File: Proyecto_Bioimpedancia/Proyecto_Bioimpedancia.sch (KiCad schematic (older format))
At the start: 53 parts

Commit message: Esquematico con Huellas
Anexado huella pulsador
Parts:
- SW?: footprint (none) -> Huellas:KPT_1187B
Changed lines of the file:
@@
 F 0 "SW?" H 8150 2810 50  0000 C CNN
 F 1 "SW_PUSH" H 8000 2620 50  0000 C CNN
-F 2 "" H 8000 2700 50  0000 C CNN
+F 2 "Huellas:KPT_1187B" H 8000 2700 50  0001 C CNN
 F 3 "" H 8000 2700 50  0000 C CNN
 	1    8000 2700

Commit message: Esquematico Actualizado
Cambios Sugeridos y división en sub-bloques
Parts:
- removed R? (x2): 10K, Resistors_SMD:R_0805_HandSoldering, symbol 10K
- added J? (x2): Jumper, Pin_Headers:Pin_Header_Straight_1x02_Pitch2.54mm, symbol Jumper
- added R? (x2): 10K, Resistors_SMD:R_0805_HandSoldering, symbol 10K
- D1: renamed from D?; footprint (none) -> LEDs:LED_0805
- R5: renamed from R?; value R_Small -> R_CAL
- U5: renamed from U?; footprint TO_SOT_Packages_SMD:SOT-223-3Lead_TabPin2 -> TO_SOT_Packages_SMD:SOT-223
- gave numbers to parts that had none: 47
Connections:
- net labels added: FEEDBACK_A2, RFB_AD5933, SIGNAL_A1, SIGNAL_A2, VIN_AD5933, VOUT_AD5933
- net labels removed: OUT_OPAMB, RFB
- wire segments 151 -> 158
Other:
- note added: "Amplicador A2"
- note added: "Amplificador A1"
- note added: "Bioimpedanciometro"
- note added: "Conector Bootloader"
- note added: "Conector Progrmador \ndel Microcontrolador"
- note added: "Microcontrolador"
- note added: "Oscilador AD5933"
- note added: "Pines de Alimentación y Control"
- note added: "Pulsador Reset"
- note added: "Regulador"
- note added: "Resistencias Pull-up"
- note added: "Señal de Reloj Externo"
- note added: "Switch Medida Bioimpedancia"
- moved on the sheet: C1, C10, C11, C12, C13, C2, C20, C3, C4, D1, P1, R1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

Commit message: Diseño Mejorado 10/05/2017
Diagrama mas explicativo con señales mas claras
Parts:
- added J1: Jumper_Calibration, Pin_Headers:Pin_Header_Straight_1x02_Pitch2.54mm, symbol Jumper
- R5: value R_CAL -> R_GAIN; footprint (none) -> Resistors_SMD:R_0805_HandSoldering
- R8: footprint (none) -> Resistors_SMD:R_0805_HandSoldering
- W1, W2, W3, W4, W5, W6: footprint (none) -> Measurement_Points:Measurement_Point_Round-TH_Small
- Y1: footprint Huellas:AMB3_Crystal_5mm_x_3,2mm_16M -> Crystals:Crystal_SMD_Abracon_ABM3-2pin_5.0x3.2mm_HandSoldering
- gave numbers to parts that had none: 4
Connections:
- net labels added: CTRL_MCLK, CTRL_SWITCH
- net labels removed: ADC2, ADC3, IN_OPAMB, OUT_OPAM1, VIN, VOUT
- wire segments 158 -> 160
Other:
- note added: "Amplificador A2"
- note added: "Electrodos de Contacto y R de Calibración"
- note added: "Oscilador AD5933 (MCLK)"
- note added: "Quemador Bootloader"
- note added: "Señales Analogicas (Medición)"
- note removed: "Amplicador A2"
- note removed: "Conector Bootloader"
- note removed: "Oscilador AD5933"
- note removed: "Señales Analogicos"
- moved on the sheet: P3, P4
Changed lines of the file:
@@
 	1    0    0    -1
 $EndComp
-Text Notes 2450 650  0    118  ~ 0
-Señales Analogicos
 $Comp
 L 0,1uF C15
@@
 MCLK
 Text Label 8150 1450 0    39   ~ 0
-ADC3
+CTRL_MCLK
 Text Label 8800 2700 0    39   ~ 0
-ADC3
+CTRL_MCLK
 Text Label 8800 2900 0    39   ~ 0
 GND
@@
 SIGNAL_A1
 Text Label 4000 1350 0    39   ~ 0
-ADC2
+CTRL_SWITCH
 Text Label 4250 1550 0    39   ~ 0
 AGND
@@
 ADC1
 Text Label 8150 1350 0    39   ~ 0
-ADC2
+CTRL_SWITCH
 Text Label 8150 1750 0    39   ~ 0
 RESET
@@
 F 0 "R8" H 5530 1370 50  0000 L CNN
 F 1 "RCAL" H 5250 1350 50  0000 L CNN
-F 2 "" H 5500 1350 50  0000 C CNN
+F 2 "Resistors_SMD:R_0805_HandSoldering" H 5500 1350 50  0001 C CNN
 F 3 "" H 5500 1350 50  0000 C CNN
 	1    5500 1350
@@
 P 1550 2450
 F 0 "R5" H 1580 2470 50  0000 L CNN
-F 1 "R_CAL" H 1580 2410 50  0000 L CNN
-F 2 "" H 1550 2450 50  0000 C CNN
+F 1 "R_GAIN" H 1580 2410 50  0000 L CNN
+F 2 "Resistors_SMD:R_0805_HandSoldering" H 1550 2450 50  0001 C CNN
 F 3 "" H 1550 2450 50  0000 C CNN
 	1    1550 2450
@@
 F 0 "Y1" H 6700 2800 50  0000 C CNN
 F 1 "AMB3_16M" H 6700 2600 50  0000 C CNN
-F 2 "Huellas:AMB3_Crystal_5mm_x_3,2mm_16M" H 6700 2700 50  0001 C CNN
+F 2 "Crystals:Crystal_SMD_Abracon_ABM3-2pin_5.0x3.2mm_HandSoldering" H 6700 2700 50  0001 C CNN
 F 3 "" H 6700 2700 50  0000 C CNN
 	1    6700 2700
@@
 L CONN_01X02 P3
 U 1 1 59144527
-P 7000 4650
-F 0 "P3" H 7000 4800 50  0000 C CNN
-F 1 "CONN_01X02" V 7100 4650 50  0000 C CNN
-F 2 "Socket_Strips:Socket_Strip_Straight_1x02_Pitch2.54mm" H 7000 4650 50  0001 C CNN
-F 3 "" H 7000 4650 50  0000 C CNN
-	1    7000 4650
+P 7000 4500
+F 0 "P3" H 7000 4650 50  0000 C CNN
+F 1 "CONN_01X02" V 7100 4500 50  0000 C CNN
+F 2 "Socket_Strips:Socket_Strip_Straight_1x02_Pitch2.54mm" H 7000 4500 50  0001 C CNN
+F 3 "" H 7000 4500 50  0000 C CNN
+	1    7000 4500
 	1    0    0    -1
 $EndComp
@@
 L CONN_01X02 P4
 U 1 1 59144600
-P 7900 4650
-F 0 "P4" H 7900 4800 50  0000 C CNN
-F 1 "CONN_01X02" V 8000 4650 50  0000 C CNN
-F 2 "Socket_Strips:Socket_Strip_Straight_1x02_Pitch2.54mm" H 7900 4650 50  0001 C CNN
-F 3 "" H 7900 4650 50  0000 C CNN
-	1    7900 4650
-	1    0    0    -1
-$EndComp
-Text Label 7350 4600 0    39   ~ 0
+P 8400 5350
+F 0 "P4" H 8400 5500 50  0000 C CNN
+F 1 "CONN_01X02" V 8500 5350 50  0000 C CNN
+F 2 "Socket_Strips:Socket_Strip_Straight_1x02_Pitch2.54mm" H 8400 5350 50  0001 C CNN
+F 3 "" H 8400 5350 50  0000 C CNN
+	1    8400 5350
+	1    0    0    -1
+$EndComp
+Text Label 7850 5300 0    39   ~ 0
 Z_UK
-Text Label 7350 4700 0    39   ~ 0
-IN_OPAMB
-Text Label 6350 4600 0    39   ~ 0
+Text Label 7850 5400 0    39   ~ 0
+SIGNAL_A2
+Text Label 6350 4450 0    39   ~ 0
 V_FUENTE
-Text Label 6350 4700 0    39   ~ 0
+Text Label 6350 4550 0    39   ~ 0
 AGND
 $Comp
@@
 F 0 "W1" H 1300 4670 50  0000 C CNN
 F 1 "TEST_1P" H 1300 4600 50  0000 C CNN
-F 2 "" H 1500 4400 50  0000 C CNN
+F 2 "Measurement_Points:Measurement_Point_Round-TH_Small" H 1500 4400 50  0001 C CNN
 F 3 "" H 1500 4400 50  0000 C CNN
 	1    1300 4400
@@
 F 0 "W2" H 1650 4670 50  0000 C CNN
 F 1 "TEST_1P" H 1650 4600 50  0000 C CNN
-F 2 "" H 1850 4400 50  0000 C CNN
+F 2 "Measurement_Points:Measurement_Point_Round-TH_Small" H 1850 4400 50  0001 C CNN
 F 3 "" H 1850 4400 50  0000 C CNN
 	1    1650 4400
@@
 F 0 "W3" H 2000 4670 50  0000 C CNN
 F 1 "TEST_1P" H 2000 4600 50  0000 C CNN
-F 2 "" H 2200 4400 50  0000 C CNN
+F 2 "Measurement_Points:Measurement_Point_Round-TH_Small" H 2200 4400 50  0001 C CNN
 F 3 "" H 2200 4400 50  0000 C CNN
 	1    2000 4400
@@
 F 0 "W4" H 2350 4670 50  0000 C CNN
 F 1 "TEST_1P" H 2350 4600 50  0000 C CNN
-F 2 "" H 2550 4400 50  0000 C CNN
+F 2 "Measurement_Points:Measurement_Point_Round-TH_Small" H 2550 4400 50  0001 C CNN
 F 3 "" H 2550 4400 50  0000 C CNN
 	1    2350 4400
@@
 $EndComp
 Text Label 1300 5100 1    39   ~ 0
-OUT_OPAM1
+SIGNAL_A1
 Text Label 1650 5100 1    39   ~ 0
-VOUT
+VOUT_AD5933
 Text Label 2000 5100 1    39   ~ 0
-IN_OPAMB
+SIGNAL_A2
 Text Label 2350 5100 1    39   ~ 0
 MCLK
@@
 F 0 "W5" H 2700 4670 50  0000 C CNN
 F 1 "TEST_1P" H 2700 4600 50  0000 C CNN
-F 2 "" H 2900 4400 50  0000 C CNN
+F 2 "Measurement_Points:Measurement_Point_Round-TH_Small" H 2900 4400 50  0001 C CNN
 F 3 "" H 2900 4400 50  0000 C CNN
 	1    2700 4400
@@
 $EndComp
 Text Label 2700 5100 1    39   ~ 0
-VIN
+VIN_AD5933
 $Comp
 L TEST_1P W6
@@
 F 0 "W6" H 3100 4670 50  0000 C CNN
 F 1 "TEST_1P" H 3100 4600 50  0000 C CNN
-F 2 "" H 3300 4400 50  0000 C CNN
+F 2 "Measurement_Points:Measurement_Point_Round-TH_Small" H 3300 4400 50  0001 C CNN
 F 3 "" H 3300 4400 50  0000 C CNN
 	1    3100 4400
@@
 3V3
 $Comp
-L 10K R?
+L 10K R10
 U 1 1 591650D4
 P 1200 5800
-F 0 "R?" H 1230 5820 50  0000 L CNN
+F 0 "R10" H 1230 5820 50  0000 L CNN
 F 1 "10K" H 1230 5760 50  0000 L CNN
 F 2 "Resistors_SMD:R_0805_HandSoldering" H 1130 5720 50  0001 C CNN
@@
 $EndComp
 $Comp
-L 10K R?
+L 10K R11
 U 1 1 59165125
 P 1500 5800
-F 0 "R?" H 1530 5820 50  0000 L CNN
+F 0 "R11" H 1530 5820 50  0000 L CNN
 F 1 "10K" H 1530 5760 50  0000 L CNN
 F 2 "Resistors_SMD:R_0805_HandSoldering" H 1430 5720 50  0001 C CNN
@@
 SCL
 $Comp
-L Jumper J?
+L Jumper J2
 U 1 1 591891AD
 P 8250 1550
-F 0 "J?" V 8200 1600 50  0000 L CNN
+F 0 "J2" V 8200 1600 50  0000 L CNN
 F 1 "Jumper" V 8200 1250 50  0000 L CNN
 F 2 "Pin_Headers:Pin_Header_Straight_1x02_Pitch2.54mm" H 8250 1550 50  0001 C CNN
@@
 $EndComp
 $Comp
-L Jumper J?
+L Jumper J3
 U 1 1 5918A975
 P 8250 1650
-F 0 "J?" V 8200 1700 50  0000 L CNN
+F 0 "J3" V 8200 1700 50  0000 L CNN
 F 1 "Jumper" V 8200 1350 50  0000 L CNN
 F 2 "Pin_Headers:Pin_Header_Straight_1x02_Pitch2.54mm" H 8250 1650 50  0001 C CNN
@@
 Pulsador Reset
 Text Notes 8950 3400 0    59   ~ 0
-Oscilador AD5933
+Oscilador AD5933 (MCLK)
 Text Notes 9300 2200 0    59   ~ 0
 Bioimpedanciometro
@@
 Amplificador A1
 Text Notes 3000 2350 0    59   ~ 0
-Amplicador A2
+Amplificador A2
 Text Notes 4400 900  0    59   ~ 0
 Switch Medida Bioimpedancia
 Text Notes 4550 4050 0    59   ~ 0
-Conector Bootloader
+Quemador Bootloader
 Text Notes 4150 5000 0    59   ~ 0
 Conector Progrmador \ndel Microcontrolador
@@
 	9250 2900 8800 2900
 Wire Wire Line
-	7900 1450 8150 1450
-Wire Wire Line
 	1350 1600 2250 1600
 Wire Wire Line
@@
 Wire Wire Line
 	6800 1050 6500 1050
-Wire Wire Line
-	7900 1350 8150 1350
 Wire Wire Line
 	7900 1250 8150 1250
@@
 	10300 5100 10550 5100
 Wire Wire Line
-	7700 4600 7350 4600
-Wire Wire Line
-	7700 4700 7350 4700
-Wire Wire Line
-	6800 4600 6350 4600
-Wire Wire Line
-	6350 4700 6800 4700
+	8200 5300 7850 5300
+Wire Wire Line
+	8200 5400 7850 5400
+Wire Wire Line
+	6800 4450 6350 4450
+Wire Wire Line
+	6350 4550 6800 4550
 Wire Wire Line
 	9900 5450 10300 5450
@@
 	650  5250 3750 5250
 Wire Notes Line
-	8850 4000 8850 5700
-Wire Notes Line
-	8850 5700 6100 5700
-Wire Notes Line
-	6100 5700 6100 4000
-Wire Notes Line
-	6100 4000 8850 4000
-Wire Wire Line
-	6400 5150 6950 5150
-Text Label 6400 5150 0    59   ~ 0
-GND
-Text Label 6950 5150 0    59   ~ 0
-AGND
+	6100 4000 8900 4000
+Wire Wire Line
+	7800 4550 8350 4550
+Text Label 7800 4550 0    59   ~ 0
+GND
+Text Label 8350 4550 0    59   ~ 0
+AGND
+Wire Wire Line
+	7900 1450 8150 1450
+Wire Wire Line
+	7900 1350 8150 1350
+Wire Notes Line
+	8900 4000 8900 4900
+Wire Notes Line
+	8900 4900 6100 4900
+Wire Notes Line
+	6100 4900 6100 4000
+Text Notes 2450 650  0    118  ~ 0
+Señales Analogicas (Medición)
+Wire Notes Line
+	8900 4950 8900 5700
+Wire Notes Line
+	8900 5700 6100 5700
+Wire Notes Line
+	6100 5700 6100 4950
+Wire Notes Line
+	6100 4950 8900 4950
+Text Notes 6550 5050 0    60   ~ 0
+Electrodos de Contacto y R de Calibración
+$Comp
+L Jumper J1
+U 1 1 5918524B
+P 6800 5250
+F 0 "J1" V 6750 5300 50  0000 L CNN
+F 1 "Jumper_Calibration" V 6900 5150 50  0000 L CNN
+F 2 "Pin_Headers:Pin_Header_Straight_1x02_Pitch2.54mm" H 6800 5250 50  0001 C CNN
+F 3 "" H 6800 5250 50  0000 C CNN
+	1    6800 5250
+	0    1    1    0
+$EndComp
+Wire Wire Line
+	6900 5250 7150 5250
+Wire Wire Line
+	6700 5250 6400 5250
+Text Label 7150 5250 0    39   ~ 0
+FEEDBACK_A2
+Text Label 6400 5250 0    39   ~ 0
+SIGNAL_A2
 $EndSCHEMATC

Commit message: Segregación Bioimpedanciometro
Faltaria el cambio del regulador
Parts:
- removed C14, C3: 0,1uF, Capacitors_SMD:C_0805_HandSoldering, symbol 0,1uF
- removed C17: 10uF, Capacitors_SMD:C_0805_HandSoldering, symbol 10uF
- removed R12: R0, Capacitors_SMD:C_0805_HandSoldering, symbol R0
- added C2: 10uF, Capacitors_SMD:C_0805_HandSoldering, symbol 10uF
- added J2: Jumper, Pin_Headers:Pin_Header_Straight_1x02_Pitch2.54mm, symbol Jumper
- renumbered C12 to C11, C13 to C12, C11 to C13, C15 to C14, C16 to C15, C18 to C16, C19 to C17, C20 to C18, C2 to C3, J2 to J3, J3 to J4, P2 to P1, P1 to P2, R3 to R1, R8 to R10, R9 to R11, R4 to R2, R10 to R3, R11 to R4, R1 to R5, R2 to R6, R5 to R7, R6 to R8, R7 to R9
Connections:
- wire segments 160 -> 164
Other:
- note added: "Electrodos de Contacto \n"
- note added: "Resistencia de Ganancia A2"
- note removed: "Electrodos de Contacto y R de Calibración"
- moved on the sheet: C14, C16, D1, J1, P4, R13

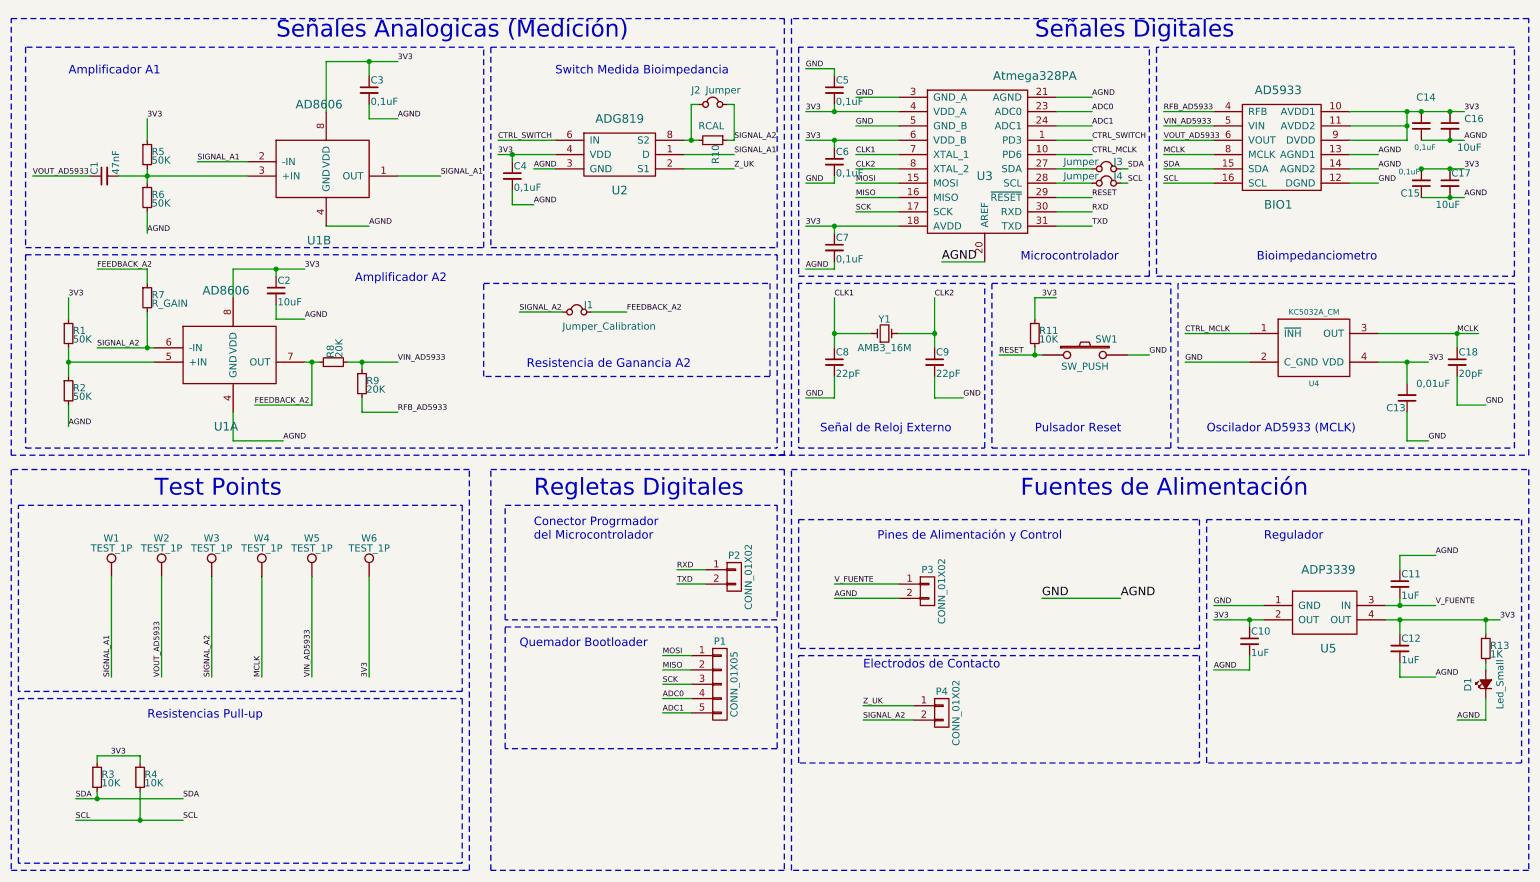
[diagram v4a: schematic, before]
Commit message: Layout casi terminado
Faltan tierras y polarización solamente
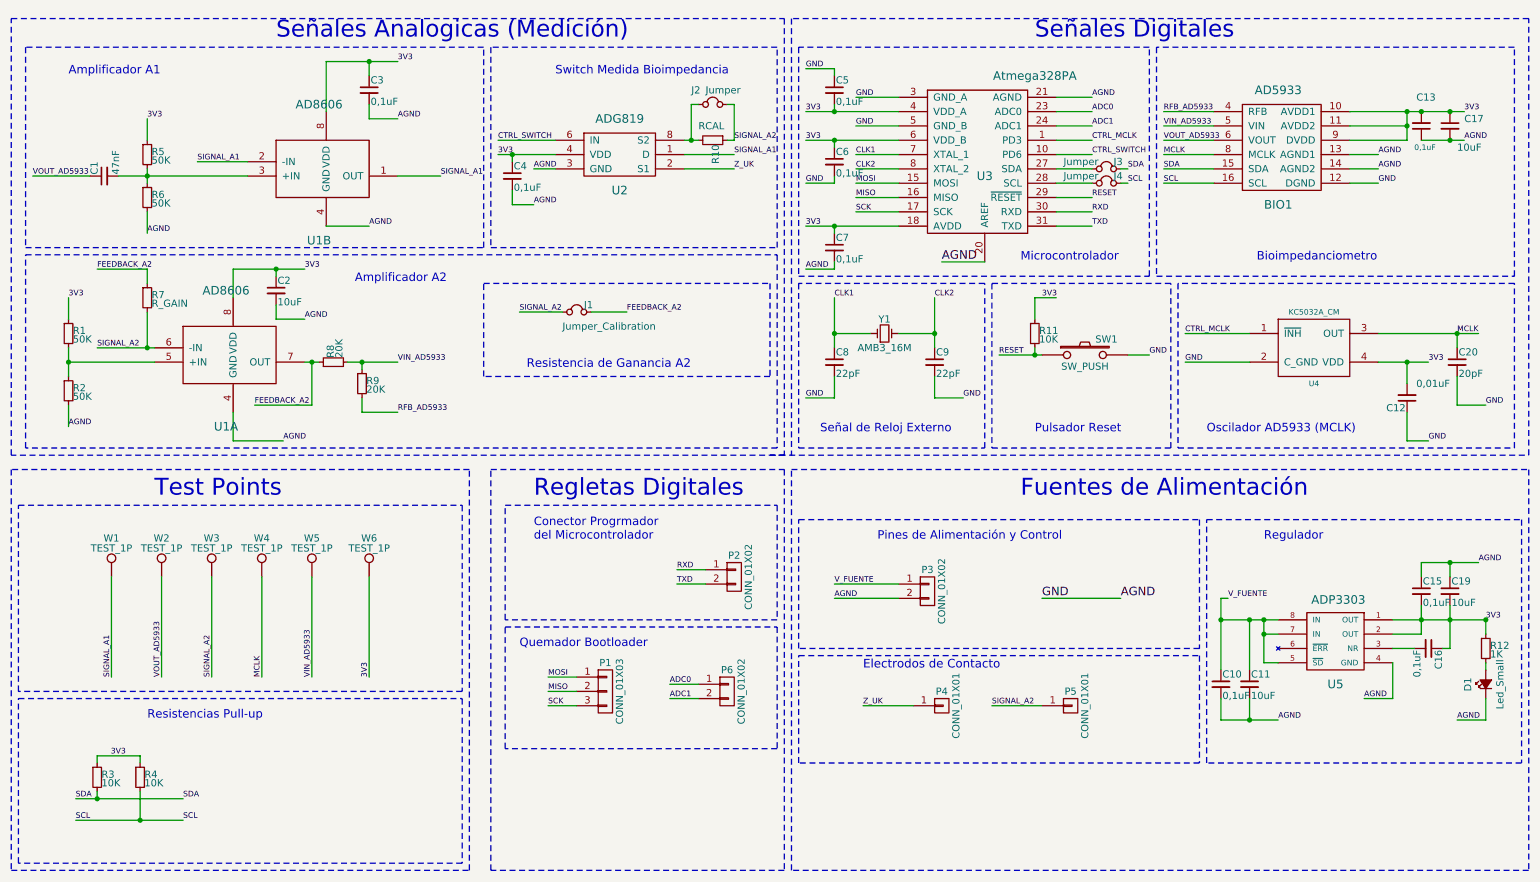
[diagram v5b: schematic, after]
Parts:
- removed C10, C11, C12: 1uF, Capacitors_SMD:C_0805_HandSoldering, symbol 1uF
- removed C17: 10uF, Capacitors_SMD:C_0805_HandSoldering, symbol 10uF
- removed P1: CONN_01X05, Socket_Strips:Socket_Strip_Straight_1x05_Pitch2.54mm, symbol CONN_01X05
- removed P4: CONN_01X02, Socket_Strips:Socket_Strip_Straight_1x02_Pitch2.54mm, symbol CONN_01X02
- removed U5: ADP3339, TO_SOT_Packages_SMD:SOT-223, symbol ADP3339
- added C10, C16: 0,1uF, Capacitors_SMD:C_0805_HandSoldering, symbol 0,1uF
- added C11, C19: 10uF, Capacitors_SMD:C_0805_HandSoldering, symbol 10uF
- added P1: CONN_01X03, Socket_Strips:Socket_Strip_Straight_1x03_Pitch2.54mm, symbol CONN_01X03
- added P4, P5: CONN_01X01, Socket_Strips:Socket_Strip_Straight_1x01_Pitch2.54mm, symbol CONN_01X01
- added P6: CONN_01X02, Socket_Strips:Socket_Strip_Straight_1x02_Pitch2.54mm, symbol CONN_01X02
- added U5: ADP3303, Housings_SOIC:SOIC-8_3.9x4.9mm_Pitch1.27mm, symbol ADP3303
- renumbered C13 to C12, C14 to C13, C16 to C17, C18 to C20, R13 to R12
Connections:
- net 3V3: now also C16.1, C19.2, U5.1 (OUT), U5.2 (OUT)
- net ADC0: now also P6.1 (P1)
- net ADC1: now also P6.2 (P2)
- net AGND: now also C10.2, C11.2, C19.1, U5.4 (GND)
- net CTRL_MCLK: now also U3.1 (PD3); no longer U3.10 (PD6)
- net CTRL_SWITCH: now also U3.10 (PD6); no longer U3.1 (PD3)
- net MISO: now also P1.2 (P2)
- net MOSI: now also P1.1 (P1)
- net SCK: now also P1.3 (P3)
- net SIGNAL_A2: now also P5.1 (P1)
- net V_FUENTE: now also C10.1, C11.1, U5.5 (~SD), U5.7 (IN), U5.8 (IN)
- net Z_UK: now also P4.1 (P1)
- new net: C16.2, U5.3 (NR)

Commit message: VersionFinal 2.0
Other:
- note added: "No olvidar \nEEPROM para \nla memoria \nde datos \n24LC64 que \nse halla en \nel datasheet \ndel ad5933 \n !!!!!"
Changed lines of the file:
@@
 	1    0    0    -1
 $EndComp
+Wire Notes Line
+	10350 1450 10350 2250
+Wire Notes Line
+	10350 2250 11050 2250
+Wire Notes Line
+	11050 2250 11050 1450
+Wire Notes Line
+	11050 1450 10350 1450
+Text Notes 10500 2050 0    39   ~ 0
+No olvidar \nEEPROM para \nla memoria \nde datos \n24LC64  que \nse halla en \nel datasheet \ndel ad5933 \n !!!!!
 $EndSCHEMATC

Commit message: Version con BOM File aprobado
Falta solo la RAM
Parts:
- removed C8, C9: 22pF, Capacitors_SMD:C_0805_HandSoldering, symbol 22pF
- removed D1: Led_Small, LEDs:LED_0805, symbol Led_Small
- added C8, C9: 18pF, Capacitors_SMD:C_0805_HandSoldering, symbol 18pF
- added D2: Led_Small_Reg, LEDs:LED_0805, symbol Led_Small_Reg
- U3: footprint Housings_QFP:LQFP-32_7x7mm_Pitch0.8mm -> Housings_QFP:TQFP-32_7x7mm_Pitch0.8mm
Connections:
- net AGND: now also C8.2, C9.2, D2.1 (K)
- net CLK1: now also C8.1
- net CLK2: now also C9.1
- net at R12.2: now also D2.2 (A)
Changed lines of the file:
@@
 F 0 "U3" H 7400 900 60  0000 C CNN
 F 1 "Atmega328PA" H 7750 1600 60  0000 C CNN
-F 2 "Housings_QFP:LQFP-32_7x7mm_Pitch0.8mm" H 7400 1250 60  0001 C CNN
+F 2 "Housings_QFP:TQFP-32_7x7mm_Pitch0.8mm" H 7400 1250 60  0001 C CNN
 F 3 "" H 7400 1250 60  0000 C CNN
 	1    7400 1250
@@
 Text Label 6350 4550 0    39   ~ 0
 AGND
-$Comp
-L 22pF C9
-U 1 1 5914EB40
-P 7050 2900
-F 0 "C9" H 7060 2970 50  0000 L CNN
-F 1 "22pF" H 7060 2820 50  0000 L CNN
-F 2 "Capacitors_SMD:C_0805_HandSoldering" H 6960 2870 50  0001 C CNN
-F 3 "" H 7060 2970 50  0000 C CNN
-F 4 "399-1113-2-ND" H 7160 3070 39  0001 C CNN "CAP CER 22PF 50V C0G/NP0 0805"
-	1    7050 2900
-	1    0    0    -1
-$EndComp
-$Comp
-L 22pF C8
-U 1 1 5914EFAD
-P 6350 2900
-F 0 "C8" H 6360 2970 50  0000 L CNN
-F 1 "22pF" H 6360 2820 50  0000 L CNN
-F 2 "Capacitors_SMD:C_0805_HandSoldering" H 6260 2870 50  0001 C CNN
-F 3 "" H 6360 2970 50  0000 C CNN
-F 4 "399-1113-2-ND" H 6460 3070 39  0001 C CNN "CAP CER 22PF 50V C0G/NP0 0805"
-	1    6350 2900
-	1    0    0    -1
-$EndComp
 Text Label 6350 2450 0    39   ~ 0
 CLK1
@@
 Text Label 3100 5100 1    39   ~ 0
 3V3
-$Comp
-L Led_Small D1
-U 1 1 5918C53C
-P 10900 5150
-F 0 "D1" H 10850 5275 50  0000 L CNN
-F 1 "Led_Small" H 10725 5050 50  0000 L CNN
-F 2 "LEDs:LED_0805" V 10900 5150 50  0001 C CNN
-F 3 "" V 10900 5150 50  0000 C CNN
-	1    10900 5150
-	0    -1   -1   0
-$EndComp
 $Comp
 L 1K R12
@@
 Text Notes 10500 2050 0    39   ~ 0
 No olvidar \nEEPROM para \nla memoria \nde datos \n24LC64  que \nse halla en \nel datasheet \ndel ad5933 \n !!!!!
+$Comp
+L Led_Small_Reg D2
+U 1 1 591D296A
+P 10900 5150
+F 0 "D2" H 10850 5275 50  0000 L CNN
+F 1 "Led_Small_Reg" H 10450 5050 50  0000 L CNN
+F 2 "LEDs:LED_0805" V 10900 5150 50  0001 C CNN
+F 3 "" V 10900 5150 50  0000 C CNN
+F 4 "475-1410-2-ND" H 10950 5375 60  0001 C CNN "LED GREEN DIFFUSED 0805 SMD"
+	1    10900 5150
+	0    -1   -1   0
+$EndComp
+$Comp
+L 18pF C9
+U 1 1 591D60A8
+P 7050 2900
+F 0 "C9" H 7060 2970 50  0000 L CNN
+F 1 "18pF" H 7060 2820 50  0000 L CNN
+F 2 "Capacitors_SMD:C_0805_HandSoldering" H 6960 2870 50  0001 C CNN
+F 3 "" H 7060 2970 50  0000 C CNN
+F 4 "399-1113-2-ND" H 7160 3070 39  0001 C CNN "CAP CER 22PF 50V C0G/NP0 0805"
+	1    7050 2900
+	1    0    0    -1
+$EndComp
+$Comp
+L 18pF C8
+U 1 1 591D65F1
+P 6350 2900
+F 0 "C8" H 6360 2970 50  0000 L CNN
+F 1 "18pF" H 6360 2820 50  0000 L CNN
+F 2 "Capacitors_SMD:C_0805_HandSoldering" H 6260 2870 50  0001 C CNN
+F 3 "" H 6360 2970 50  0000 C CNN
+F 4 "399-1113-2-ND" H 6460 3070 39  0001 C CNN "CAP CER 22PF 50V C0G/NP0 0805"
+	1    6350 2900
+	1    0    0    -1
+$EndComp
 $EndSCHEMATC

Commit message: Vias corregidas
Falta regulador
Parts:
- removed P4, P5: CONN_01X01, Socket_Strips:Socket_Strip_Straight_1x01_Pitch2.54mm, symbol CONN_01X01
- added P4, P5: CONN_01X02, Socket_Strips:Socket_Strip_Straight_1x02_Pitch2.54mm, symbol CONN_01X02
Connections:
- net SIGNAL_A2: now also P5.1 (P1), P5.2 (P2)
- net Z_UK: now also P4.1 (P1), P4.2 (P2)
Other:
- note added: "El AD8606 se modifico por el \nAD8652 por la disponibilidad \nen Analog Device"
